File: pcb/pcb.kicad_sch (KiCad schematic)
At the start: 25 parts, among them J1 Conn_02x08_Top_Bottom, SW1 CherryMX_LED, SW2 CherryMX_LED, SW3 1241.1100.7095, SW4 SW_SPST, U1 ICM7211AMIPL, U2 ICM7211AMIPL, U3 ATTINY44A, U4 NL37WZ14USG, U5 CD74ACT139E, U6 MAX5035BUSA+, Y1 Crystal

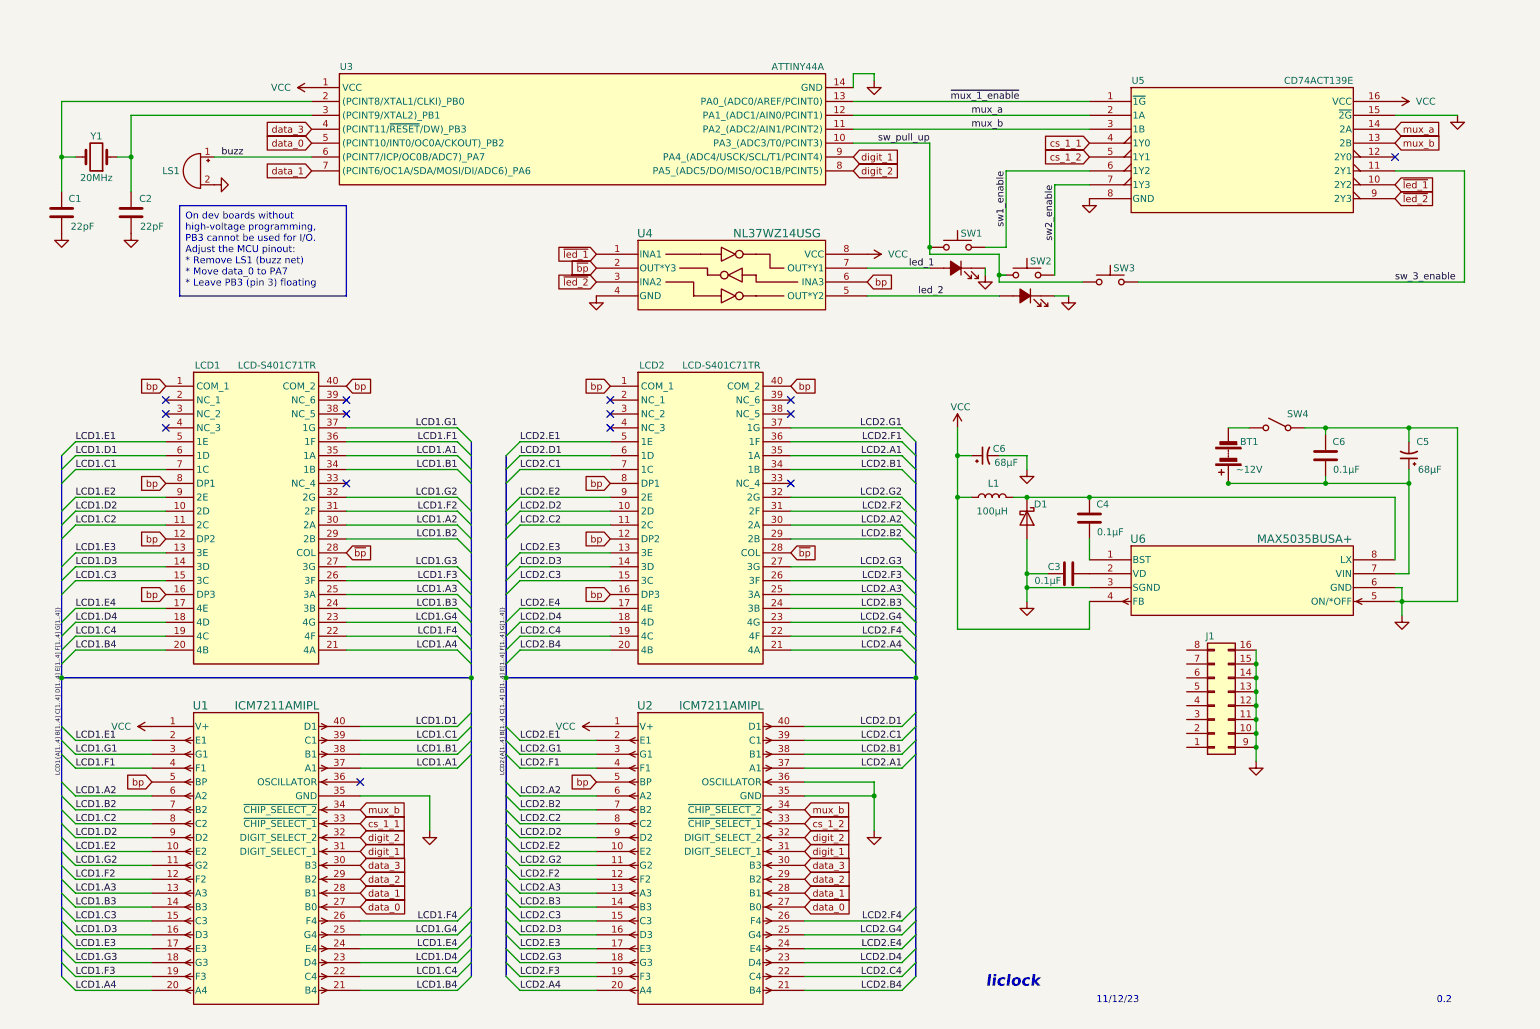
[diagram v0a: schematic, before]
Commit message: Migrate to attiny84a
Signed-off-by: Michael Darr <michael.e.darr@gmail.com>
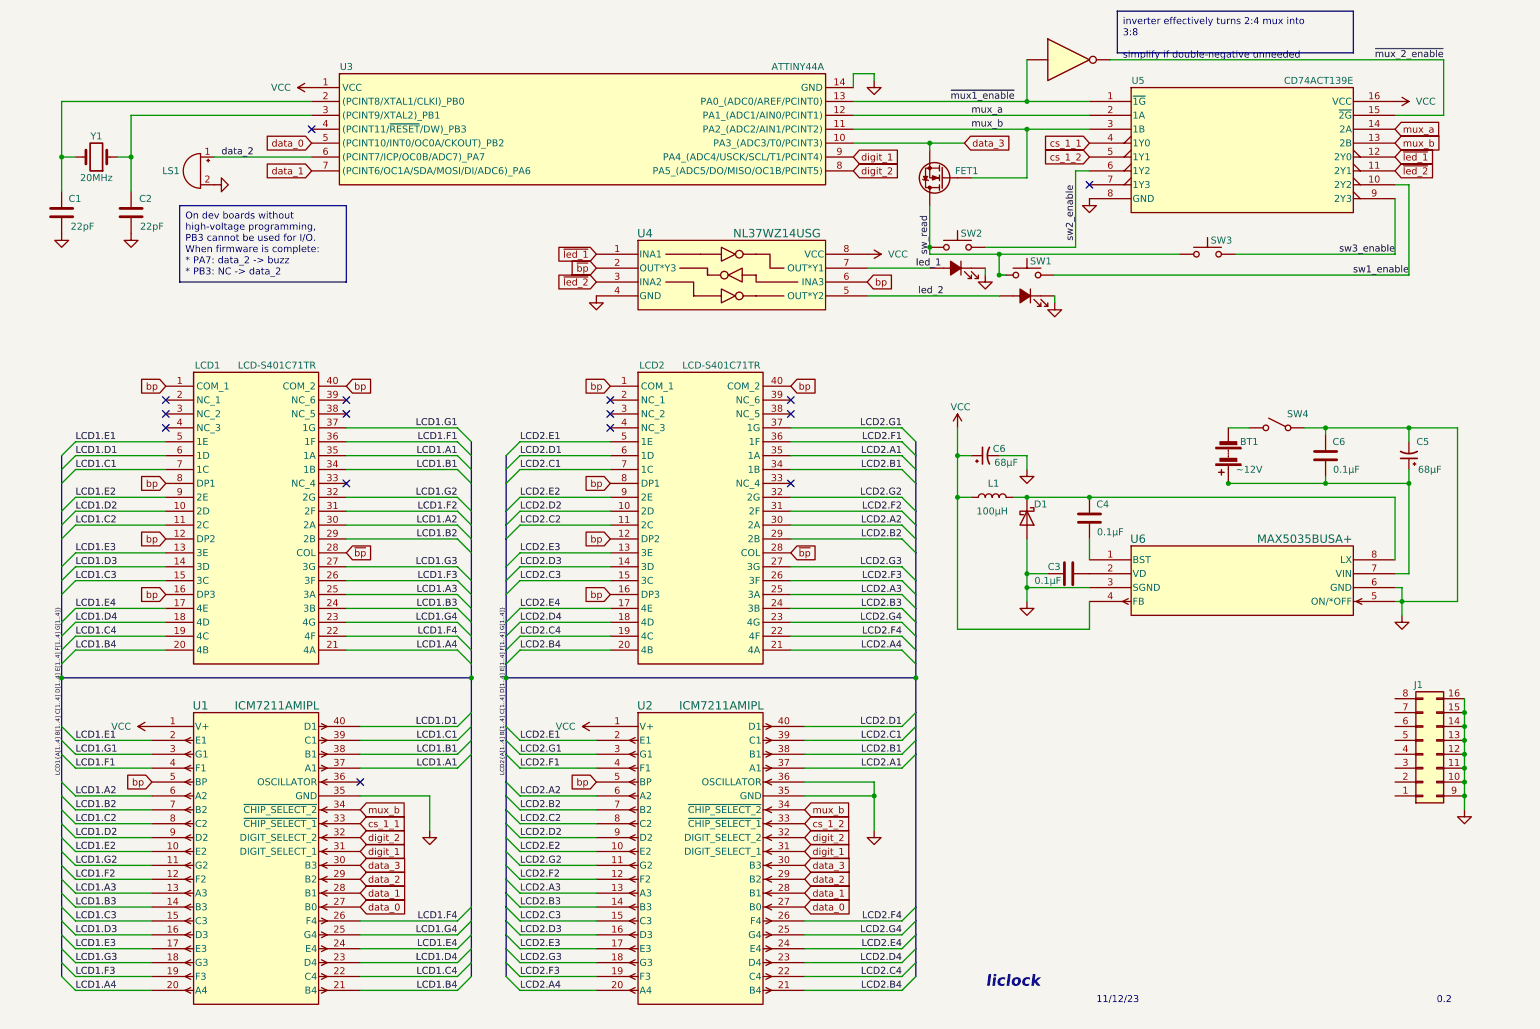
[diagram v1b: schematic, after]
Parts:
- added FET1: BSP89, Package_TO_SOT_SMD:SOT-223-3_TabPin2, symbol Transistor_FET:BSP89
- added U?: 74AHC04, symbol 74xx:74AHC04
- renumbered SW2 to SW1, SW1 to SW2
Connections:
- net buzz is gone; now on net data_2: LS1.1 (-), U3.6 ((PCINT7/ICP/OC0B/ADC7)_PA7)
- net GND: no longer U5.15 (~{2G})
- net data_3: now also U3.10 (PA3_(ADC3/T0/PCINT3)), FET1.3 (S); no longer U3.4 ((PCINT11/~{RESET}/DW)_PB3)
- net mux_b: now also FET1.1 (G)
- net sw1_enable: now also SW1.1, U5.10 (2Y2); no longer SW2.1, U5.6 (1Y2)
- net sw2_enable: now also SW2.1, U5.6 (1Y2); no longer SW1.1, U5.7 (1Y3)
- net ~{led_1}: now also U5.12 (2Y0); no longer U5.10 (2Y2)
- net ~{led_2}: now also U5.11 (2Y1); no longer U5.9 (2Y3)
- net sw_3_enable renamed sw_read
- net sw_read: now also SW1.2, SW2.2, FET1.2 (D); no longer U5.11 (2Y1)
- removed net sw_pull_up: SW1.2, SW2.2, SW3.2, U3.10 (PA3_(ADC3/T0/PCINT3))
- net ~{mux_1_enable} renamed ~{mux1_enable}
- net ~{mux1_enable}: now also U?.1
- new net sw3_enable: SW3.2, U5.9 (2Y3)
- new net ~{mux_2_enable}: U5.15 (~{2G}), U?.2
- no-connect marks 14 -> 15
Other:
- moved on the sheet: J1, SW3

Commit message: Update schematic
Signed-off-by: Michael Darr <michael.e.darr@gmail.com>
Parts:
- removed U5: CD74ACT139E, N16, symbol Clock-Parts:CD74ACT139E
- removed U?: 74AHC04, symbol 74xx:74AHC04
- added C1, C2, C3, C4, C5: 0.1µF, symbol Device:C
- added FET2: XP9561GI, symbol Simulation_SPICE:PMOS
- added J2: Conn_02x08_Top_Bottom, symbol Connector_Generic:Conn_02x08_Top_Bottom
- added LED1: 151033RS03000, symbol Device:LED
- added R1, R2, R3: 100Ω, symbol Device:R
- added U5: SN74AHC138DR, D16, symbol Clock-Parts:SN74AHC138DR
- C11: renamed from C1; Capacitance 22pF -> 20pF
- C12: renamed from C2; Capacitance 22pF -> 20pF
- FET1: PN (none) -> 2N7002-G
- U3: value ATTINY44A -> ATTINY84A; Arrow Part Number ATTINY44A-PU -> (none); Arrow Price/Stock https://www.arrow.com/en/products/attiny44a-pu/microchip-te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 -> (none); Manufacturer_Part_Number ATTINY44A-PU -> ATTINY48A-PU; Mouser Part Number 556-ATTINY44A-PU -> (none); Mouser Price/Stock https://www.mouser.co.uk/ProductDetail/Microchip-Technology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 -> (none)
- renumbered C6 to C10, C3 to C7, C4 to C8, C5 to C9, SW2 to SW1, SW1 to SW2
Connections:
- net GND: now also C7.1, C1.2, C2.2, C3.2, C4.2, C5.2, J2.10 (Pin_10), J2.11 (Pin_11), J2.12 (Pin_12), J2.13 (Pin_13), J2.14 (Pin_14), J2.15 (Pin_15), J2.16 (Pin_16), J2.9 (Pin_9), U5.4 (~{G}2A), U5.5 (~{G}2B), U5.8 (GND); no longer C7.2
- net VCC: now also C1.1, C2.1, C3.1, C4.1, C5.1, FET2.3 (S), J2.8 (Pin_8), U5.16 (VCC), U5.6 (G1)
- net cs_1_1: now also J1.8 (Pin_8), U5.15 (Y0)
- net cs_1_2: now also J1.7 (Pin_7), U5.14 (Y1)
- net data_0: now also J1.1 (Pin_1)
- net data_1: now also J1.2 (Pin_2), U3.6 ((PCINT7/ICP/OC0B/ADC7)_PA7); no longer U3.7 ((PCINT6/OC1A/SDA/MOSI/DI/ADC6)_PA6)
- net data_2: now also J1.3 (Pin_3), U3.7 ((PCINT6/OC1A/SDA/MOSI/DI/ADC6)_PA6); no longer LS1.1 (-), U3.6 ((PCINT7/ICP/OC0B/ADC7)_PA7)
- net data_3: now also FET1.2 (D), J1.4 (Pin_4); no longer FET1.3 (S)
- net digit_1: now also J1.5 (Pin_5)
- net digit_2: now also J1.6 (Pin_6)
- net led_1: now also R1.1; no longer SW1.4 (A)
- net led_2: now also R2.1; no longer SW2.4 (A)
- net mux_a: now also J2.7 (Pin_7), U5.1 (A)
- net mux_b: now also J2.6 (Pin_6), U5.2 (B)
- net sw3_enable: now also U5.7 (Y7)
- net sw_read: now also FET1.3 (S); no longer FET1.2 (D)
- net ~{bp}: now also J2.4 (Pin_4)
- net ~{led_1}: now also J2.3 (Pin_3), U5.11 (Y4)
- net ~{led_2}: now also J2.2 (Pin_2), U5.10 (Y5)
- net at BT1.1 (+), C10.2, C9.1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: now also FET2.2 (G)
- net at BT1.2 (-), SW4.2 (B): now also R3.1
- net at U6.2 (VD): now also C7.2; no longer C7.1
- net sw1_enable renamed ~{sw2_enable}
- net ~{sw2_enable}: now also U5.13 (Y2)
- net sw2_enable renamed ~{sw1_enable}
- net ~{sw1_enable}: now also U5.9 (Y6)
- net ~{mux1_enable} renamed mux_c
- net mux_c: now also J2.5 (Pin_5), U5.3 (C)
- new net: LED1.1 (K), R3.2
- new net: R1.2, SW1.4 (A)
- new net: FET2.1 (D), LED1.2 (A)
- new net: R2.2, SW2.4 (A)
- new net buzz: J2.1 (Pin_1), LS1.1 (-), U5.12 (Y3)
- no-connect marks 15 -> 14
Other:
- note added: "0.4"
- note added: "12/0/23"
- note added: "Cn decouples Un"
- note removed: "0.2"
- note removed: "11/12/23"
- moved on the sheet: BT1, C10, C11, C12, C6, C7, C8, C9, D1, FET1, J1, L1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

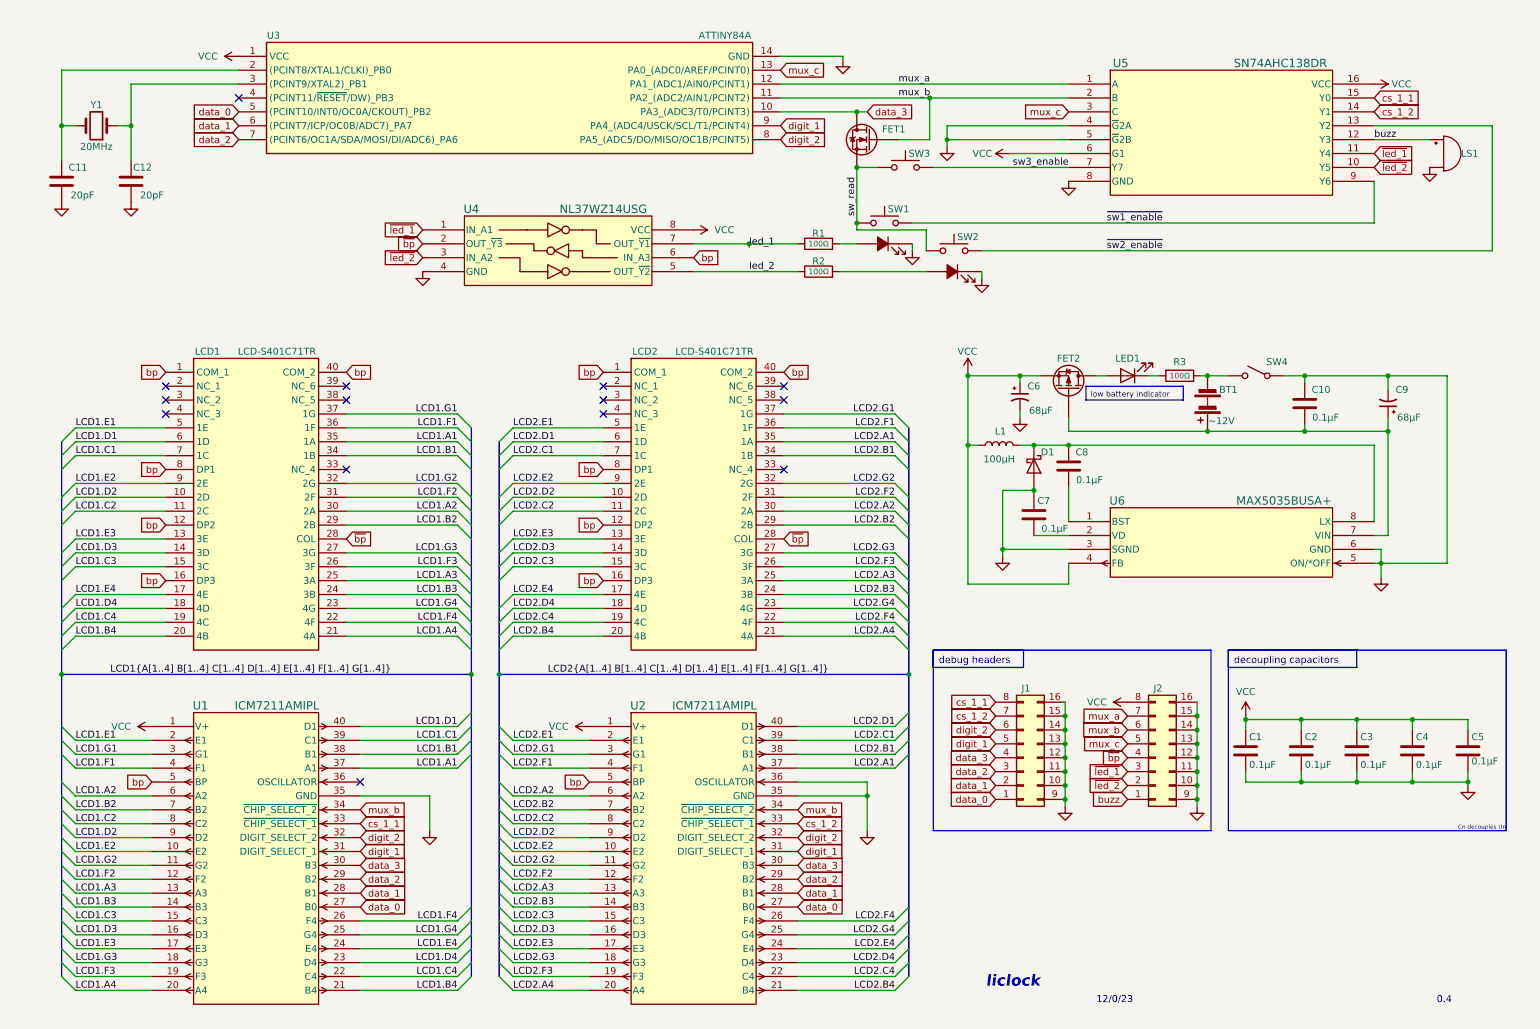
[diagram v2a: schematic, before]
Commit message: Improve signal integrity
Signed-off-by: Michael Darr <michael.e.darr@gmail.com>
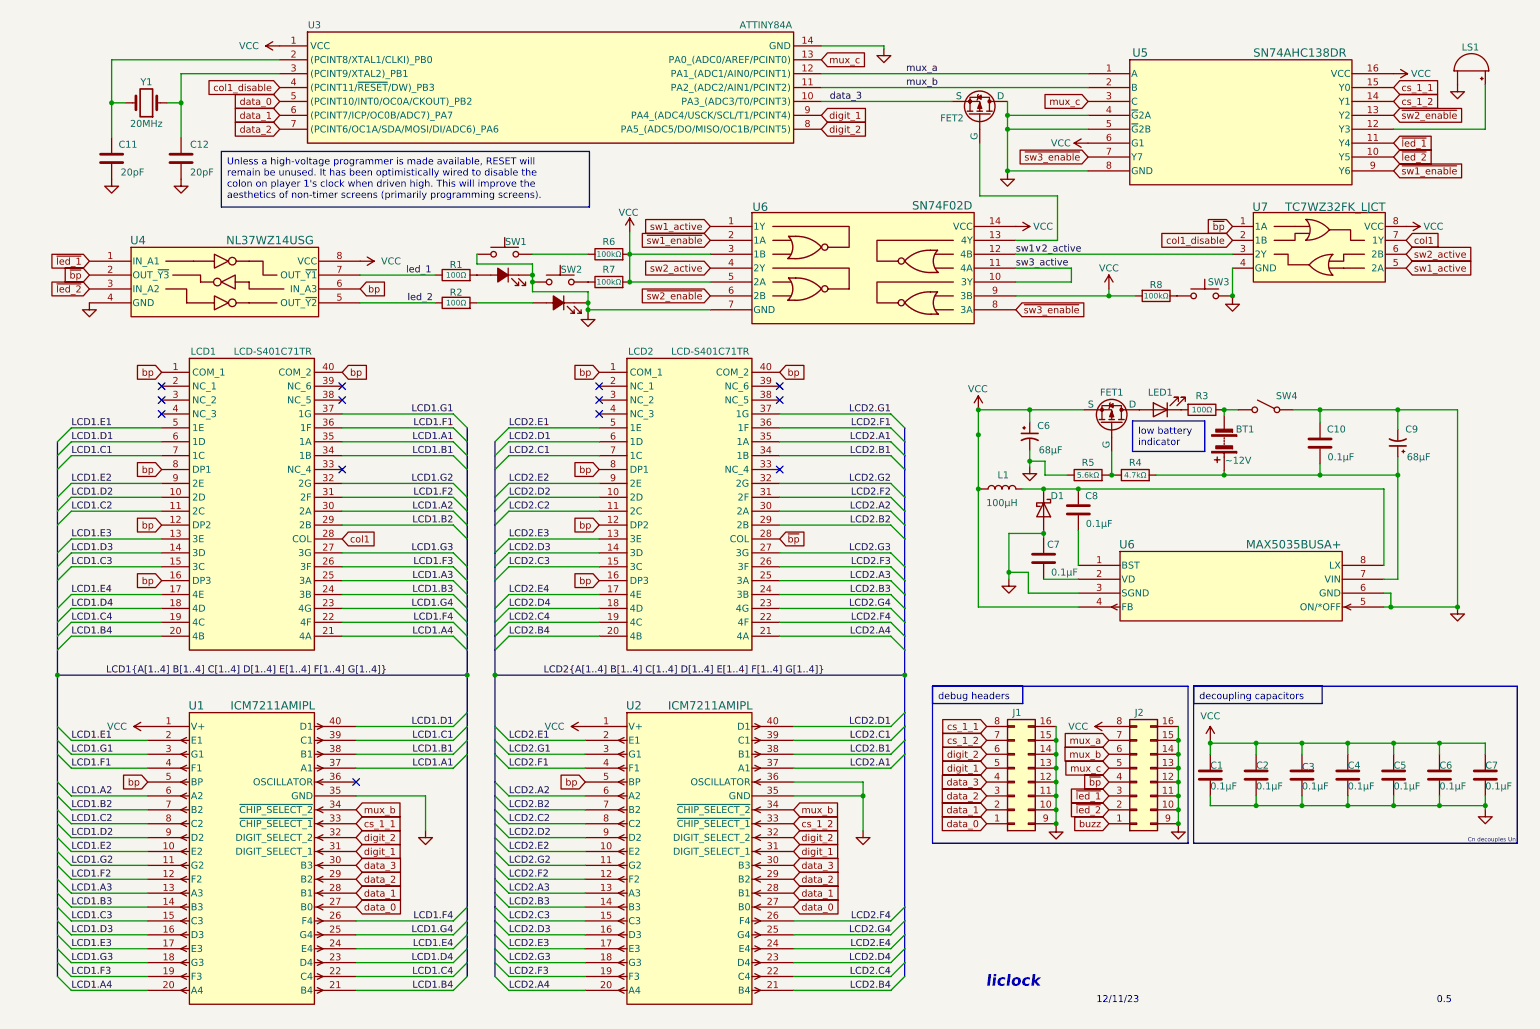
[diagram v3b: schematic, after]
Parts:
- removed FET1: BSP89, Package_TO_SOT_SMD:SOT-223-3_TabPin2, symbol Transistor_FET:BSP89
- added C6, C7: 0.1µF, symbol Device:C
- added FET2: XP9561GI, symbol Simulation_SPICE:PMOS
- added R4: 4.7kΩ, symbol Device:R
- added R5: 5.6kΩ, symbol Device:R
- added R6, R7, R8: 100kΩ, symbol Device:R
- added U6: SN74F02D, D14, symbol Clock-Parts:SN74F02D
- added U7: TC7WZ32FK_LJCT, US8_TOS, symbol Clock-Parts:TC7WZ32FK_LJCT
- renumbered FET2 to FET1
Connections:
- net GND: now also SW1.2, SW2.2, SW3.2, C6.2, C7.2, FET2.1 (D), R5.1, U6.7 (GND), U7.4 (GND)
- net VCC: now also C6.1, C7.1, R6.2, R7.2, R8.2, U6.14 (VCC), U6.3 (1B), U6.5 (2A), U6.9 (3B), U7.8 (VCC)
- net buzz: no longer LS1.1 (-), U5.12 (Y3)
- net data_3: now also FET2.3 (S)
- net ~{bp}: now also U7.1 (1A); no longer LCD1.28 (COL)
- net ~{sw1_enable}: now also U6.2 (1A); no longer SW1.1
- net ~{sw2_enable}: now also U6.6 (2B); no longer SW2.1
- net at BT1.1 (+), C10.2, C9.1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: now also R4.2; no longer FET1.2 (G)
- net col1_disable: now reaches U3.4 ((PCINT11/~{RESET}/DW)_PB3)
- net col1_disable: now also U7.2 (1B)
- net sw3_enable renamed ~{sw3_enable}
- net ~{sw3_enable}: now also U6.8 (3A); no longer SW3.2
- removed net sw_read: SW1.2, SW2.2, SW3.1
- new net: R8.1, SW3.1
- new net: R6.1, SW1.1
- new net: LS1.1 (-), U5.12 (Y3)
- new net: FET2.2 (G), U6.13 (4Y)
- new net: FET1.2 (G), R4.1, R5.2
- new net: R7.1, SW2.1
- new net col1: LCD1.28 (COL), U7.7 (1Y)
- new net sw1_active: U6.1 (1Y), U7.5 (2A)
- new net sw1∨2_active: U6.12 (4B), U7.3 (2Y)
- new net sw2_active: U6.4 (2Y), U7.6 (2B)
- new net sw3_active: U6.10 (3Y), U6.11 (4A)
- no-connect marks 14 -> 13
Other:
- note added: "0.5"
- note added: "12/11/23"
- note removed: "0.4"
- note removed: "12/0/23"
- moved on the sheet: BT1, C1, C10, C11, C12, C2, C3, C4, C5, C6, C7, C8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
